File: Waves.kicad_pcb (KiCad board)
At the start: 4 copper layers, 49.8 x 106.5 mm, 151 parts, among them J1 AudioJack2_SwitchT, J10 AudioJack2_SwitchT, J11 Conn_01x04_Male, J12 Conn_01x04_Male, J13 AudioJack2_SwitchT, J14 AudioJack2_SwitchT, J15 Conn_02x05_Odd_Even, J2 AudioJack2_SwitchT, J3 AudioJack2_SwitchT, J4 AudioJack2_SwitchT, J5 AudioJack2_SwitchT, J6 AudioJack2_SwitchT, J7 AudioJack2_SwitchT, J8 AudioJack2_SwitchT, J9 AudioJack2_SwitchT, Q1 BC847, Q2 BC847, Q3 BC847, Q4 BC847, Q5 BC847, Q6 BC847, SW1 SW_Push, SW2 Rotary_Encoder_Switch, SW3 SW_Push_LED, SW4 SW_Push_LED, SW5 SW_Push_LED, SW6 SW_Push_LED, U1 STM32G431, U2 AT25xxx, U3 IPS240x240, U4 PCM5100, U5 TL072, U6 R-78E3.3-0.5, U7 LD2981ABU33TR, U8 MCP6004, U9 MCP6004, Y1 8MHz

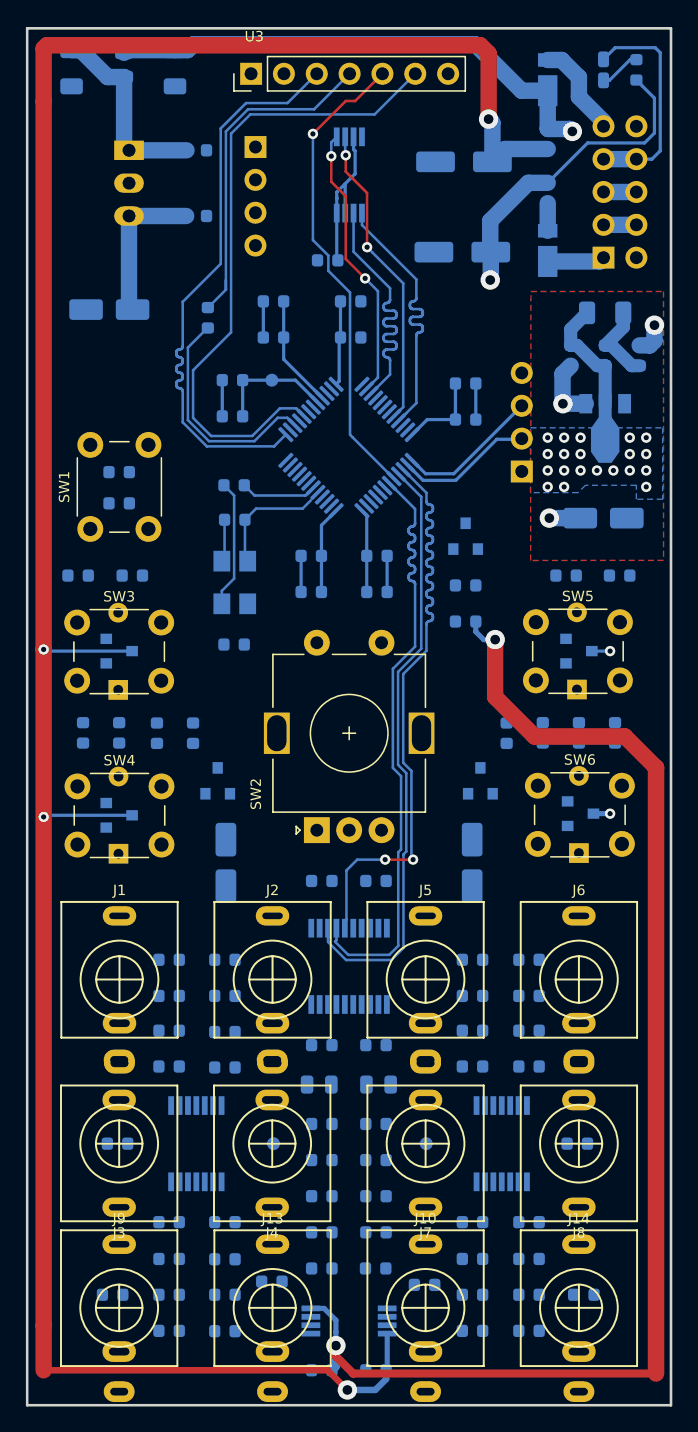
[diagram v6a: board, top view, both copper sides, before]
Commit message: Routed I2C and analog power.
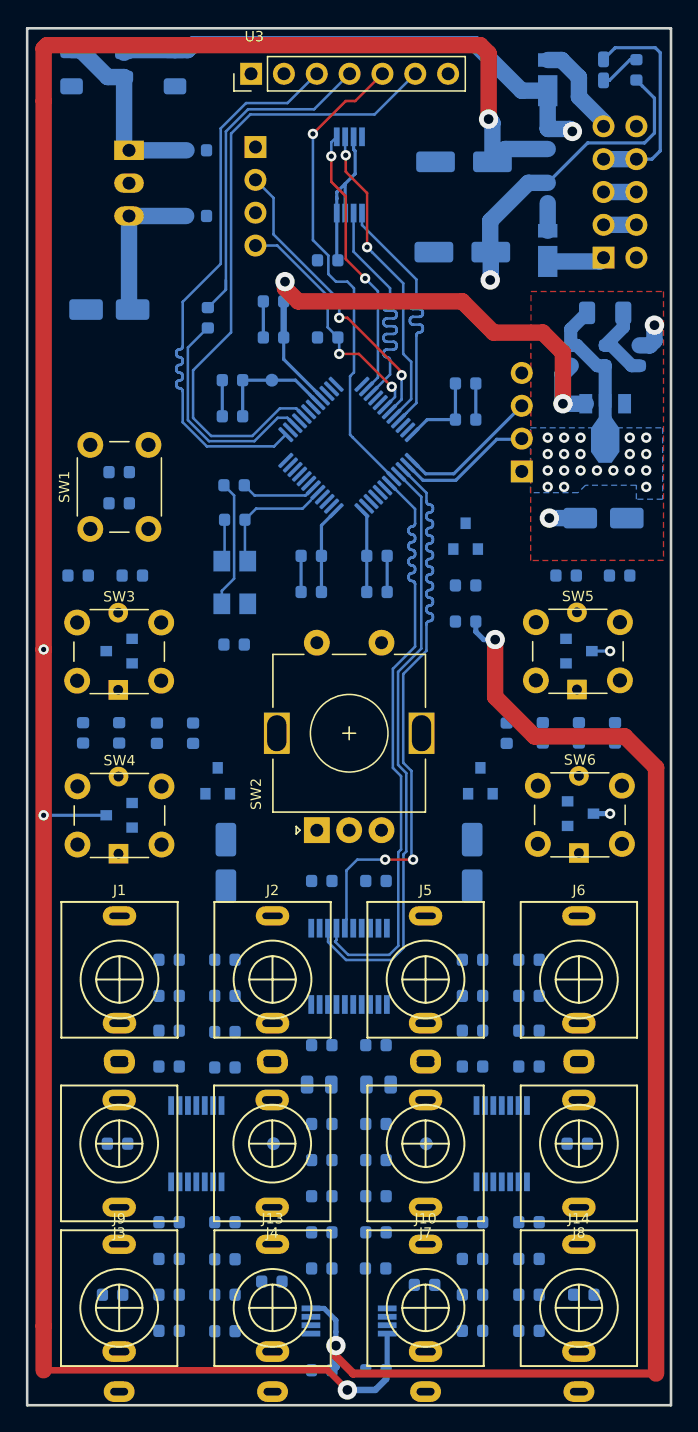
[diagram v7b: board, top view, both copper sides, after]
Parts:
- moved R3 3.31 mm to (125.2, 72.3)
- moved R4 3.31 mm to (125.2, 69.5)
- turned Q2 to 180 degrees
- turned Q4 to 180 degrees
- turned R21 to 90 degrees
- turned R22 to 0 degrees
- turned R51 to 270 degrees
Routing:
- net +3.3VA: track 16.1 -> 45.7 mm, vias 2 -> 3
- net I2C_SCL: track 0.00 -> 23.4 mm, vias 0 -> 2
- net I2C_SDA: track 0.00 -> 19.3 mm, vias 0 -> 2
- net +12V: track 283.5 -> 274.9 mm
- net +3V3: track 50.8 -> 44.2 mm
- net TFT_RES: track 36.6 -> 37.3 mm
- net MEM_MISO: track 23.8 -> 24.3 mm

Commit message: More power routing.
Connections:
- C51 pad 1: CV4B -> CV3B
- C52 pad 1: CV3B -> CV4B
- R49 pad 1: CV4B -> CV3B
- R50 pad 1: CV3B -> CV4B
- U9 pad 14: CV3B -> CV4B
- U9 pad 8: CV4B -> CV3B
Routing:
- net +3V3: track 44.2 -> 51.2 mm
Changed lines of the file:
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@@
     (thickness 1.6)
     (drawings 75)
-    (tracks 1006)
+    (tracks 1011)
     (zones 0)
     (modules 151)
@@
   )
   (setup
-    (last_trace_width 0.5)
+    (last_trace_width 0.25)
     (user_trace_width 0.2)
     (user_trace_width 0.4)
@@
     (fp_line (start -1.2 2.5) (end 2.2 2.5) (layer B.Fab) (width 0.15))
     (pad 14 smd rect (at 2.95 1.95 270) (size 1.45 0.45) (layers B.Cu B.Paste B.Mask)
-      (net 22 CV3B))
+      (net 23 CV4B))
     (pad 13 smd rect (at 2.95 1.3 270) (size 1.45 0.45) (layers B.Cu B.Paste B.Mask)
       (net 89 "Net-(C52-Pad2)"))
@@
       (net 88 "Net-(C51-Pad2)"))
     (pad 8 smd rect (at 2.95 -1.95 270) (size 1.45 0.45) (layers B.Cu B.Paste B.Mask)
-      (net 23 CV4B))
+      (net 22 CV3B))
     (pad 7 smd rect (at -2.95 -1.95 270) (size 1.45 0.45) (layers B.Cu B.Paste B.Mask)
       (net 21 CV2B))
@@
       (net 89 "Net-(C52-Pad2)"))
     (pad 1 smd roundrect (at -0.7875 0) (size 0.875 0.95) (layers B.Cu B.Paste B.Mask) (roundrect_rratio 0.25)
-      (net 22 CV3B))
+      (net 23 CV4B))
     (model ${KISYS3DMOD}/Resistor_SMD.3dshapes/R_0603_1608Metric.wrl
       (at (xyz 0 0 0))
@@
       (net 88 "Net-(C51-Pad2)"))
     (pad 1 smd roundrect (at -0.7875 0 180) (size 0.875 0.95) (layers B.Cu B.Paste B.Mask) (roundrect_rratio 0.25)
-      (net 23 CV4B))
+      (net 22 CV3B))
     (model ${KISYS3DMOD}/Resistor_SMD.3dshapes/R_0603_1608Metric.wrl
       (at (xyz 0 0 0))
@@
       (net 89 "Net-(C52-Pad2)"))
     (pad 1 smd roundrect (at -0.7875 0) (size 0.875 0.95) (layers B.Cu B.Paste B.Mask) (roundrect_rratio 0.25)
-      (net 22 CV3B))
+      (net 23 CV4B))
     (model ${KISYS3DMOD}/Capacitor_SMD.3dshapes/C_0603_1608Metric.wrl
       (at (xyz 0 0 0))
@@
       (net 88 "Net-(C51-Pad2)"))
     (pad 1 smd roundrect (at -0.7875 0 180) (size 0.875 0.95) (layers B.Cu B.Paste B.Mask) (roundrect_rratio 0.25)
-      (net 23 CV4B))
+      (net 22 CV3B))
     (model ${KISYS3DMOD}/Capacitor_SMD.3dshapes/C_0603_1608Metric.wrl
       (at (xyz 0 0 0))
@@
   (segment (start 121.8185 72.263) (end 121.8185 73.949734) (width 0.25) (layer B.Cu) (net 4))
   (segment (start 121.8185 73.949734) (end 124.22135 76.352584) (width 0.25) (layer B.Cu) (net 4))
-  (segment (start 121.8185 69.469) (end 121.8185 72.263) (width 0.5) (layer B.Cu) (net 4))
   (segment (start 143.415 73.438) (end 143.415 77.387) (width 1.27) (layer F.Cu) (net 4))
   (segment (start 141.859 71.882) (end 143.415 73.438) (width 1.27) (layer F.Cu) (net 4))
@@
   (segment (start 121.92 69.3675) (end 121.8185 69.469) (width 0.5) (layer B.Cu) (net 4))
   (segment (start 121.92 67.945) (end 121.92 69.3675) (width 0.5) (layer B.Cu) (net 4))
+  (segment (start 121.8185 72.263) (end 121.8185 69.469) (width 0.25) (layer B.Cu) (net 4))
   (segment (start 138.9535 57.6835) (end 137.963 58.674) (width 1.27) (layer B.Cu) (net 8))
   (segment (start 142.24 57.6835) (end 138.9535 57.6835) (width 1.27) (layer B.Cu) (net 8))
@@
   (segment (start 124.7395 89.154) (end 124.7395 91.948) (width 0.25) (layer B.Cu) (net 72))
   (segment (start 128.2445 89.154) (end 128.2445 91.948) (width 0.25) (layer B.Cu) (net 72))
+  (segment (start 124.4345 72.263) (end 124.4345 69.469) (width 0.25) (layer B.Cu) (net 72))
+  (segment (start 124.4345 72.838) (end 124.4345 72.263) (width 0.25) (layer B.Cu) (net 72))
+  (segment (start 124.4345 74.438127) (end 124.4345 72.838) (width 0.25) (layer B.Cu) (net 72))
+  (segment (start 125.874212 75.884124) (end 125.874212 75.877839) (width 0.25) (layer B.Cu) (net 72))
+  (segment (start 125.874212 75.877839) (end 124.4345 74.438127) (width 0.25) (layer B.Cu) (net 72))
   (segment (start 117.0338 91.8614) (end 117.0338 92.8614) (width 0.2) (layer B.Cu) (net 77))
   (segment (start 117.98381 90.91139) (end 117.0338 91.8614) (width 0.2) (layer B.Cu) (net 77))
